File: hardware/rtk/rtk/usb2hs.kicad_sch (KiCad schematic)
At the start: 15 parts, among them J11 Conn_01x06_Pin, U8 USB3300-EZK, Y2 ASTX-H11-24.000MHZ-T

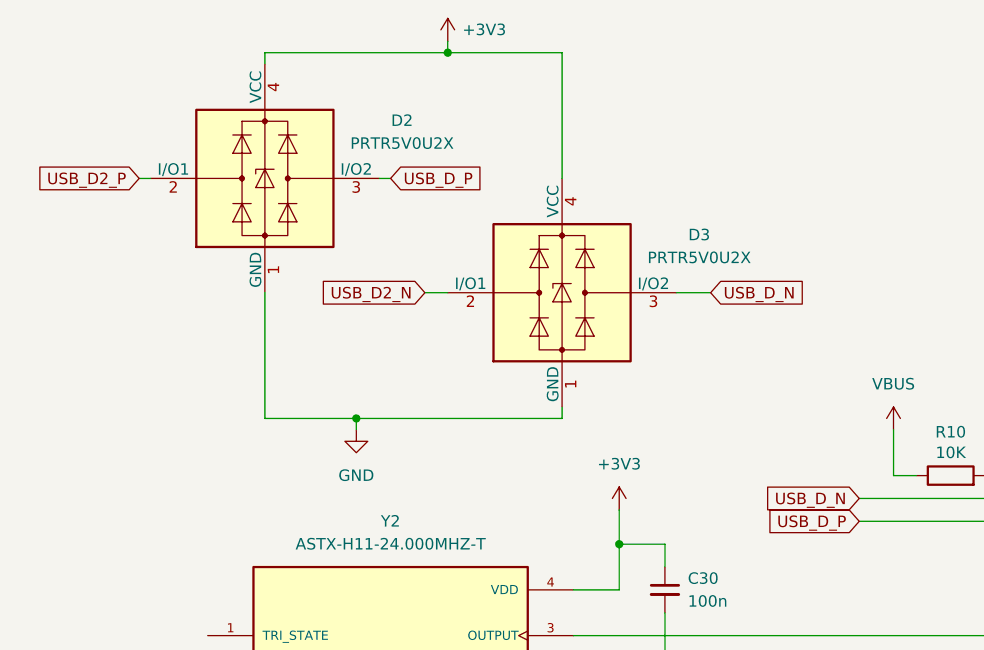
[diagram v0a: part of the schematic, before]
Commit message: Schematic fixes and PCB placement start: D2, C16/18/20, J4
- D2: PRTR5V0U2X → USBLC6-2SC6 (SOT-23-6), D3 removed
- C16/C18/C20: symbol → C_Polarized_Small, footprint → 0805 HandSolder
  (T529P106M010AAE200 polymer tant 10µF 10V)
- J4: footprint assigned (PinHeader 2.54mm, on/off switch)
- rtk.kicad_pcb: initial component placement begun
- Add USBLC6-2SC6 datasheet

Co-Authored-By: Claude Sonnet 4.6 <noreply@anthropic.com>
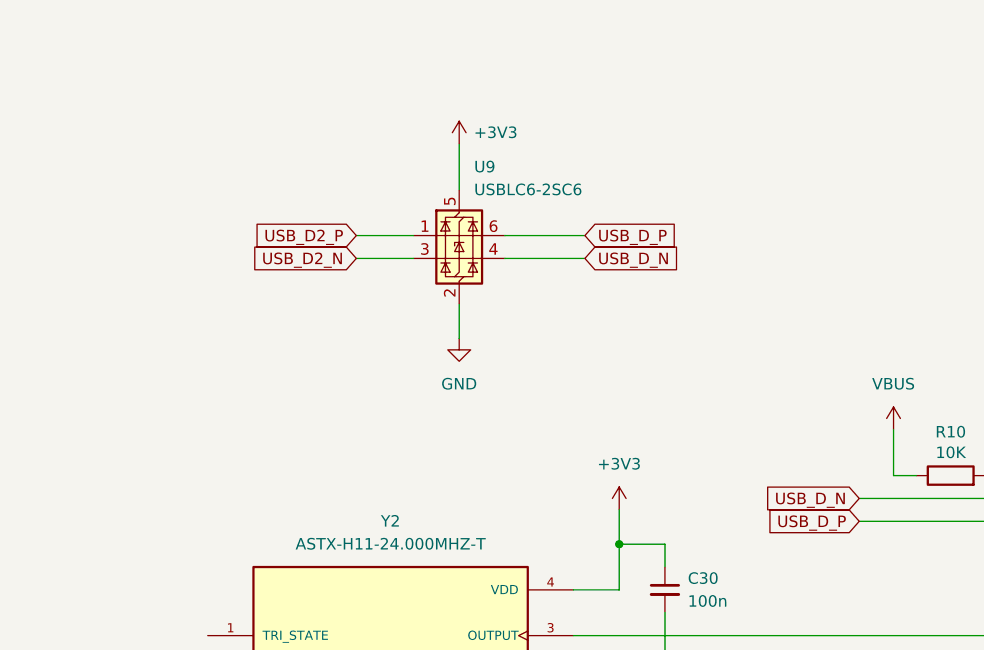
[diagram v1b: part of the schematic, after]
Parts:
- removed D2, D3: PRTR5V0U2X, Package_TO_SOT_SMD:SOT-143, symbol Power_Protection:PRTR5V0U2X
- added U9: USBLC6-2SC6, Package_TO_SOT_SMD:SOT-23-6, symbol Power_Protection:USBLC6-2SC6
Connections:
- net +3V3: now also U9.5 (VBUS)
- net GND: now also U9.2 (GND)
- net USB_D2_N: now also U9.3 (I/O2)
- net USB_D2_P: now also U9.1 (I/O1)
- net USB_D_N: now also U9.4 (I/O2)
- net USB_D_P: now also U9.6 (I/O1)

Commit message: PCB: round 1 initial placement complete
Most components in final positions; some will shift during routing.
Schematic tweaks picked up alongside. Add GCT USB4105 datasheet.

Co-Authored-By: Claude Sonnet 4.6 <noreply@anthropic.com>
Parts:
- removed C24: 100n, Capacitor_SMD:C_0805_2012Metric_Pad1.18x1.45mm_HandSolder, symbol Device:C_Small
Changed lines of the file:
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@@
-	)
-	(junction
-		(at 71.12 170.18)
-		(diameter 0)
-		(color 0 0 0 0)
 	)
 	(junction
@@
 	)
 	(junction
-		(at 71.12 180.34)
-		(diameter 0)
-		(color 0 0 0 0)
-	)
-	(junction
 		(at 59.69 170.18)
 		(diameter 0)
@@
 	(wire
 		(pts
-			(xy 71.12 177.8) (xy 71.12 180.34)
-		)
-		(stroke
-			(width 0)
-			(type default)
-		)
-	)
-	(wire
-		(pts
 			(xy 63.5 46.99) (xy 63.5 50.8)
 		)
@@
 	(wire
 		(pts
-			(xy 59.69 170.18) (xy 71.12 170.18)
-		)
-		(stroke
-			(width 0)
-			(type default)
-		)
-	)
-	(wire
-		(pts
 			(xy 38.1 166.37) (xy 38.1 170.18)
 		)
@@
 	(wire
 		(pts
-			(xy 71.12 180.34) (xy 81.28 180.34)
+			(xy 59.69 180.34) (xy 81.28 180.34)
 		)
 		(stroke
@@
 	(wire
 		(pts
-			(xy 59.69 180.34) (xy 71.12 180.34)
-		)
-		(stroke
-			(width 0)
-			(type default)
-		)
-	)
-	(wire
-		(pts
 			(xy 165.1 63.5) (xy 177.8 63.5)
 		)
@@
 	(wire
 		(pts
-			(xy 71.12 170.18) (xy 81.28 170.18)
+			(xy 59.69 170.18) (xy 81.28 170.18)
 		)
 		(stroke
@@
 		(pts
 			(xy 165.1 81.28) (xy 181.61 81.28)
-		)
-		(stroke
-			(width 0)
-			(type default)
-		)
-	)
-	(wire
-		(pts
-			(xy 71.12 170.18) (xy 71.12 172.72)
 		)
 		(stroke
@@
 					(unit 1)
 				)
-			)
-		)
-	)
-	(symbol
-		(lib_id "Device:C_Small")
-		(at 71.12 175.26 0)
-		(unit 1)
-		(body_style 1)
-		(exclude_from_sim no)
-		(in_bom yes)
-		(on_board yes)
-		(in_pos_files yes)
-		(dnp no)
-		(fields_autoplaced yes)
-		(property "Reference" "C24"
-			(at 73.66 173.9962 0)
-			(show_name no)
-			(do_not_autoplace no)
-			(effects
-				(font
-					(size 1.27 1.27)
-				)
-				(justify left)
-			)
-		)
-		(property "Value" "100n"
-			(at 73.66 176.5362 0)
-			(show_name no)
-			(do_not_autoplace no)
-			(effects
-				(font
-					(size 1.27 1.27)
-				)
-				(justify left)
-			)
-		)
-		(property "Footprint" "Capacitor_SMD:C_0805_2012Metric_Pad1.18x1.45mm_HandSolder"
-			(at 71.12 175.26 0)
-			(hide yes)
-			(show_name no)
-			(do_not_autoplace no)
-			(effects
-				(font
-					(size 1.27 1.27)
-				)
-			)
-		)
-		(property "Datasheet" ""
-			(at 71.12 175.26 0)
-			(hide yes)
-			(show_name no)
-			(do_not_autoplace no)
-			(effects
-				(font
-					(size 1.27 1.27)
-				)
-			)
-		)
-		(property "Description" "Unpolarized capacitor, small symbol"
-			(at 71.12 175.26 0)
-			(hide yes)
-			(show_name no)
-			(do_not_autoplace no)
-			(effects
-				(font
-					(size 1.27 1.27)
-				)
-			)
-		)
-		(pin "1"
-		)
-		(pin "2"
-		)
-		(instances
-			(project "rtk"
-				(path "/608e0f5f-bf55-4b10-9802-aab1430116aa/d8cc858a-b41d-4a13-a4a7-a7323237874f"
-					(reference "C24")
-					(unit 1)
-				)
